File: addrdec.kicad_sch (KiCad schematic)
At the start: 5 parts, among them U10 74LS138, U11 74HCT00, U5 74HCT02, U8 74LS04, U9 74LS27

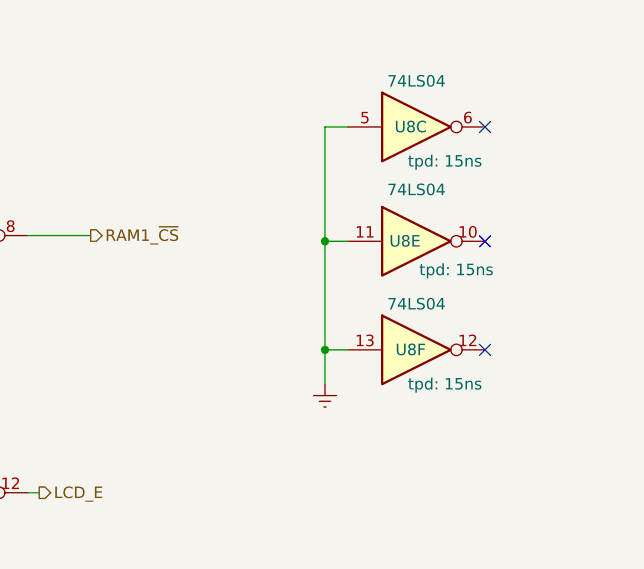
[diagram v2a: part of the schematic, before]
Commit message: fixed bugs in IRQ prio circuit
POST pass
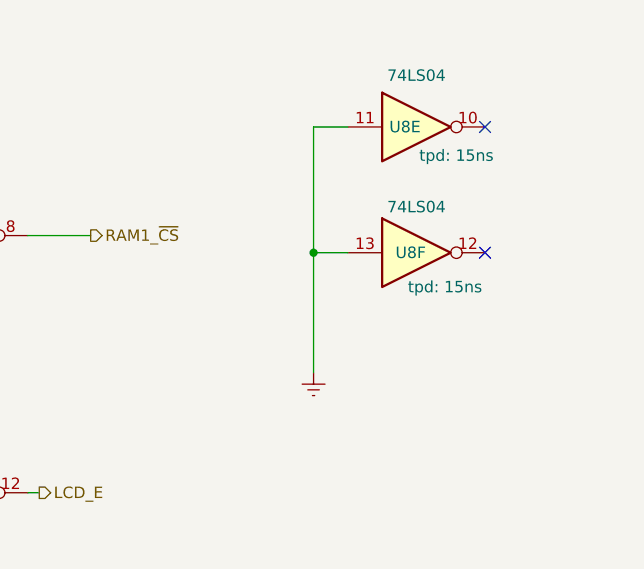
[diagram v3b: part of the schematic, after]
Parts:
- removed unit 3 of U8
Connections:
- no-connect marks 3 -> 2
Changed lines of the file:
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@@
 (kicad_sch (version 20230121) (generator eeschema)
   (paper "A4")
-  (junction (at 151.13 41.91) (diameter 0) (color 0 0 0 0)
-  )
   (junction (at 33.02 48.26) (diameter 0) (color 0 0 0 0)
   )
@@
   (junction (at 52.07 77.47) (diameter 0) (color 0 0 0 0)
   )
-  (junction (at 151.13 53.975) (diameter 0) (color 0 0 0 0)
-  )
   (junction (at 75.565 24.13) (diameter 0) (color 0 0 0 0)
   )
+  (junction (at 149.86 43.18) (diameter 0) (color 0 0 0 0)
+  )
   (junction (at 73.025 43.815) (diameter 0) (color 0 0 0 0)
   )
@@
   (junction (at 147.32 99.695) (diameter 0) (color 0 0 0 0)
   )
-  (no_connect (at 168.91 53.975))
-  (no_connect (at 168.91 41.91))
   (no_connect (at 168.91 29.21))
+  (no_connect (at 168.91 43.18))
   (bus_entry (at 27.94 82.55) (size 2.54 -2.54)
     (stroke (width 0) (type default))
@@
     (stroke (width 0) (type default))
   )
+  (wire (pts (xy 149.86 43.18) (xy 153.67 43.18))
+    (stroke (width 0) (type default))
+  )
   (bus (pts (xy 27.94 72.39) (xy 27.94 77.47))
     (stroke (width 0) (type default) (color 27 101 1 1))
@@
     (stroke (width 0) (type default))
   )
-  (wire (pts (xy 153.67 29.21) (xy 151.13 29.21))
+  (wire (pts (xy 153.67 29.21) (xy 149.86 29.21))
     (stroke (width 0) (type default))
   )
@@
   )
   (wire (pts (xy 82.55 72.39) (xy 102.87 72.39))
-    (stroke (width 0) (type default))
-  )
-  (wire (pts (xy 153.67 53.975) (xy 151.13 53.975))
     (stroke (width 0) (type default))
   )
@@
     (stroke (width 0) (type default))
   )
-  (wire (pts (xy 151.13 29.21) (xy 151.13 41.91))
+  (wire (pts (xy 149.86 43.18) (xy 149.86 56.515))
+    (stroke (width 0) (type default))
+  )
+  (wire (pts (xy 149.86 29.21) (xy 149.86 43.18))
     (stroke (width 0) (type default))
   )
@@
     (stroke (width 0) (type default))
   )
-  (wire (pts (xy 151.13 41.91) (xy 153.67 41.91))
-    (stroke (width 0) (type default))
-  )
   (wire (pts (xy 35.56 24.13) (xy 35.56 54.61))
     (stroke (width 0) (type default))
@@
     (stroke (width 0) (type default))
   )
-  (wire (pts (xy 151.13 53.975) (xy 151.13 57.785))
-    (stroke (width 0) (type default))
-  )
   (wire (pts (xy 62.865 24.13) (xy 75.565 24.13))
     (stroke (width 0) (type default))
@@
   )
   (wire (pts (xy 75.565 41.275) (xy 78.74 41.275))
-    (stroke (width 0) (type default))
-  )
-  (wire (pts (xy 151.13 41.91) (xy 151.13 53.975))
     (stroke (width 0) (type default))
   )
@@
     (effects (font (size 1.27 1.27)) (justify left))
   )
-  (hierarchical_label "LCD_E" (shape output) (at 119.38 69.85 0) (fields_autoplaced)
+  (hierarchical_label "LCD_E" (shape output) (at 119.38 69.85 0)
     (effects (font (size 1.27 1.27)) (justify left))
+    (property "tpd_LH" "56ns" (at 118.11 72.39 0) (show_name)
+      (effects (font (size 1.27 1.27) italic) (justify left))
+    )
+    (property "tpd_HL" "15ns" (at 118.11 74.041 0) (show_name)
+      (effects (font (size 1.27 1.27) italic) (justify left))
+    )
   )
   (hierarchical_label "DEV2_~{CS}" (shape output) (at 87.63 80.01 0) (fields_autoplaced)
@@
     )
   )
+  (symbol (lib_id "74xx:74LS04") (at 161.29 43.18 0) (unit 6)
+    (in_bom yes) (on_board yes) (dnp no)
+    (property "Reference" "U8" (at 160.655 43.18 0)
+      (effects (font (size 1.27 1.27)))
+    )
+    (property "Value" "74LS04" (at 161.29 38.1 0)
+      (effects (font (size 1.27 1.27)))
+    )
+    (property "Footprint" "" (at 161.29 43.18 0)
+      (effects (font (size 1.27 1.27)) hide)
+    )
+    (property "Datasheet" "http://www.ti.com/lit/gpn/sn74LS04" (at 161.29 43.18 0)
+      (effects (font (size 1.27 1.27)) hide)
+    )
+    (property "tpd" "15ns" (at 164.465 46.99 0) (show_name)
+      (effects (font (size 1.27 1.27)))
+    )
+    (pin "1")
+    (pin "2")
+    (pin "3")
+    (pin "4")
+    (pin "5")
+    (pin "6")
+    (pin "8")
+    (pin "9")
+    (pin "10")
+    (pin "11")
+    (pin "12")
+    (pin "13")
+    (pin "14")
+    (pin "7")
+    (instances
+      (project "rod6502"
+        (path "/031ea57b-8d17-4b45-87cc-c58302485ce1/4032fa43-c28c-4c35-b0ce-d5d9da6e84af"
+          (reference "U8") (unit 6)
+        )
+        (path "/031ea57b-8d17-4b45-87cc-c58302485ce1/890f0003-2042-459e-ac4a-1dd81f8fbcc6"
+          (reference "U8") (unit 6)
+        )
+      )
+    )
+  )
   (symbol (lib_id "74xx:74LS27") (at 43.18 77.47 0) (unit 2)
     (in_bom yes) (on_board yes) (dnp no)
@@
     )
   )
-  (symbol (lib_id "power:Earth") (at 151.13 57.785 0) (unit 1)
+  (symbol (lib_id "power:Earth") (at 149.86 56.515 0) (unit 1)
     (in_bom yes) (on_board yes) (dnp no) (fields_autoplaced)
-    (property "Reference" "#PWR044" (at 151.13 64.135 0)
-      (effects (font (size 1.27 1.27)) hide)
-    )
-    (property "Value" "Earth" (at 151.13 61.595 0)
-      (effects (font (size 1.27 1.27)) hide)
-    )
-    (property "Footprint" "" (at 151.13 57.785 0)
-      (effects (font (size 1.27 1.27)) hide)
-    )
-    (property "Datasheet" "~" (at 151.13 57.785 0)
+    (property "Reference" "#PWR044" (at 149.86 62.865 0)
+      (effects (font (size 1.27 1.27)) hide)
+    )
+    (property "Value" "Earth" (at 149.86 60.325 0)
+      (effects (font (size 1.27 1.27)) hide)
+    )
+    (property "Footprint" "" (at 149.86 56.515 0)
+      (effects (font (size 1.27 1.27)) hide)
+    )
+    (property "Datasheet" "~" (at 149.86 56.515 0)
       (effects (font (size 1.27 1.27)) hide)
     )
@@
     )
   )
-  (symbol (lib_id "74xx:74LS04") (at 161.29 41.91 0) (unit 5)
-    (in_bom yes) (on_board yes) (dnp no)
-    (property "Reference" "U8" (at 160.02 41.91 0)
-      (effects (font (size 1.27 1.27)))
-    )
-    (property "Value" "74LS04" (at 161.29 36.195 0)
-      (effects (font (size 1.27 1.27)))
-    )
-    (property "Footprint" "" (at 161.29 41.91 0)
-      (effects (font (size 1.27 1.27)) hide)
-    )
-    (property "Datasheet" "http://www.ti.com/lit/gpn/sn74LS04" (at 161.29 41.91 0)
-      (effects (font (size 1.27 1.27)) hide)
-    )
-    (property "tpd" "15ns" (at 165.735 45.085 0) (show_name)
-      (effects (font (size 1.27 1.27)))
-    )
-    (pin "1")
-    (pin "2")
-    (pin "3")
-    (pin "4")
-    (pin "5")
-    (pin "6")
-    (pin "8")
-    (pin "9")
-    (pin "10")
-    (pin "11")
-    (pin "12")
-    (pin "13")
-    (pin "14")
-    (pin "7")
-    (instances
-      (project "rod6502"
-        (path "/031ea57b-8d17-4b45-87cc-c58302485ce1/4032fa43-c28c-4c35-b0ce-d5d9da6e84af"
-          (reference "U8") (unit 5)
-        )
-        (path "/031ea57b-8d17-4b45-87cc-c58302485ce1/890f0003-2042-459e-ac4a-1dd81f8fbcc6"
-          (reference "U8") (unit 5)
-        )
-      )
-    )
-  )
   (symbol (lib_id "74xx:74LS04") (at 55.245 24.13 0) (unit 1)
     (in_bom yes) (on_board yes) (dnp no)
@@
     )
   )
-  (symbol (lib_id "74xx:74LS04") (at 161.29 53.975 0) (unit 6)
-    (in_bom yes) (on_board yes) (dnp no)
-    (property "Reference" "U8" (at 160.655 53.975 0)
-      (effects (font (size 1.27 1.27)))
-    )
-    (property "Value" "74LS04" (at 161.29 48.895 0)
-      (effects (font (size 1.27 1.27)))
-    )
-    (property "Footprint" "" (at 161.29 53.975 0)
-      (effects (font (size 1.27 1.27)) hide)
-    )
-    (property "Datasheet" "http://www.ti.com/lit/gpn/sn74LS04" (at 161.29 53.975 0)
-      (effects (font (size 1.27 1.27)) hide)
-    )
-    (property "tpd" "15ns" (at 164.465 57.785 0) (show_name)
-      (effects (font (size 1.27 1.27)))
-    )
-    (pin "1")
-    (pin "2")
-    (pin "3")
-    (pin "4")
-    (pin "5")
-    (pin "6")
-    (pin "8")
-    (pin "9")
-    (pin "10")
-    (pin "11")
-    (pin "12")
-    (pin "13")
-    (pin "14")
-    (pin "7")
-    (instances
-      (project "rod6502"
-        (path "/031ea57b-8d17-4b45-87cc-c58302485ce1/4032fa43-c28c-4c35-b0ce-d5d9da6e84af"
-          (reference "U8") (unit 6)
-        )
-      )
-    )
-  )
   (symbol (lib_id "power:VCC") (at 69.85 55.88 0) (unit 1)
     (in_bom yes) (on_board yes) (dnp no) (fields_autoplaced)
@@
     )
   )
-  (symbol (lib_id "74xx:74LS04") (at 161.29 29.21 0) (unit 3)
-    (in_bom yes) (on_board yes) (dnp no)
-    (property "Reference" "U8" (at 160.655 29.21 0)
-      (effects (font (size 1.27 1.27)))
-    )
-    (property "Value" "74LS04" (at 161.29 24.13 0)
+  (symbol (lib_id "74xx:74LS04") (at 161.29 29.21 0) (unit 5)
+    (in_bom yes) (on_board yes) (dnp no)
+    (property "Reference" "U8" (at 160.02 29.21 0)
+      (effects (font (size 1.27 1.27)))
+    )
+    (property "Value" "74LS04" (at 161.29 23.495 0)
       (effects (font (size 1.27 1.27)))
     )
@@
       (effects (font (size 1.27 1.27)) hide)
     )
-    (property "tpd" "15ns" (at 164.465 33.02 0) (show_name)
-      (effects (font (size 1.27 1.27)))
-    )
-    (pin "1")
-    (pin "2")
-    (pin "3")
-    (pin "4")
-    (pin "5")
-    (pin "6")
-    (pin "8")
-    (pin "9")
-    (pin "10")
-    (pin "11")
-    (pin "12")
-    (pin "13")
-    (pin "14")
-    (pin "7")
-    (instances
-      (project "rod6502"
-        (path "/031ea57b-8d17-4b45-87cc-c58302485ce1/4032fa43-c28c-4c35-b0ce-d5d9da6e84af"
-          (reference "U8") (unit 3)
+    (property "tpd" "15ns" (at 165.735 32.385 0) (show_name)
+      (effects (font (size 1.27 1.27)))
+    )
+    (pin "1")
+    (pin "2")
+    (pin "3")
+    (pin "4")
+    (pin "5")
+    (pin "6")
+    (pin "8")
+    (pin "9")
+    (pin "10")
+    (pin "11")
+    (pin "12")
+    (pin "13")
+    (pin "14")
+    (pin "7")
+    (instances
+      (project "rod6502"
+        (path "/031ea57b-8d17-4b45-87cc-c58302485ce1/4032fa43-c28c-4c35-b0ce-d5d9da6e84af"
+          (reference "U8") (unit 5)
         )
         (path "/031ea57b-8d17-4b45-87cc-c58302485ce1/890f0003-2042-459e-ac4a-1dd81f8fbcc6"
-          (reference "U8") (unit 3)
-        )
-      )
+          (reference "U8") (unit 5)
+        )
+      )

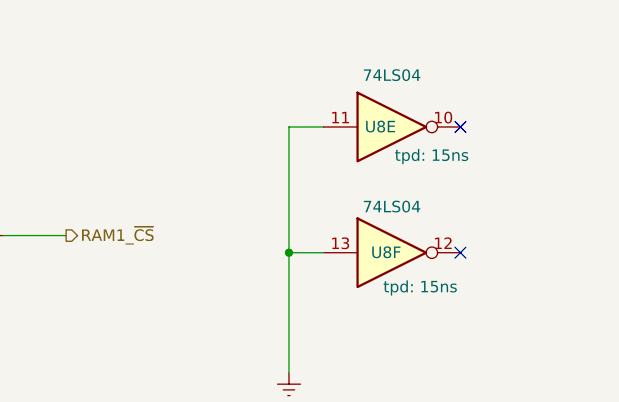
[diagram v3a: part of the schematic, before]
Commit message: output POST status on lcd display
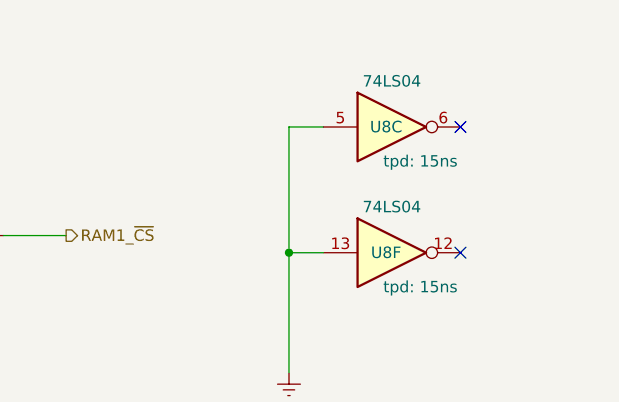
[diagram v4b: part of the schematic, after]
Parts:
- removed unit 5 of U8
- added unit 3 of U8
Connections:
- net Earth: now also U8.5
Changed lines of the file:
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@@
+    )
+  )
+  (symbol (lib_id "74xx:74LS04") (at 161.29 29.21 0) (unit 3)
+    (in_bom yes) (on_board yes) (dnp no)
+    (property "Reference" "U8" (at 160.655 29.21 0)
+      (effects (font (size 1.27 1.27)))
+    )
+    (property "Value" "74LS04" (at 161.29 24.13 0)
+      (effects (font (size 1.27 1.27)))
+    )
+    (property "Footprint" "" (at 161.29 29.21 0)
+      (effects (font (size 1.27 1.27)) hide)
+    )
+    (property "Datasheet" "http://www.ti.com/lit/gpn/sn74LS04" (at 161.29 29.21 0)
+      (effects (font (size 1.27 1.27)) hide)
+    )
+    (property "tpd" "15ns" (at 164.465 33.02 0) (show_name)
+      (effects (font (size 1.27 1.27)))
+    )
+    (pin "1")
+    (pin "2")
+    (pin "3")
+    (pin "4")
+    (pin "5")
+    (pin "6")
+    (pin "8")
+    (pin "9")
+    (pin "10")
+    (pin "11")
+    (pin "12")
+    (pin "13")
+    (pin "14")
+    (pin "7")
+    (instances
+      (project "rod6502"
+        (path "/031ea57b-8d17-4b45-87cc-c58302485ce1/4032fa43-c28c-4c35-b0ce-d5d9da6e84af"
+          (reference "U8") (unit 3)
+        )
+        (path "/031ea57b-8d17-4b45-87cc-c58302485ce1/890f0003-2042-459e-ac4a-1dd81f8fbcc6"
+          (reference "U8") (unit 3)
+        )
+      )
     )
   )
@@
         )
       )
-    )
-  )
-  (symbol (lib_id "74xx:74LS04") (at 161.29 29.21 0) (unit 5)
-    (in_bom yes) (on_board yes) (dnp no)
-    (property "Reference" "U8" (at 160.02 29.21 0)
-      (effects (font (size 1.27 1.27)))
-    )
-    (property "Value" "74LS04" (at 161.29 23.495 0)
-      (effects (font (size 1.27 1.27)))
-    )
-    (property "Footprint" "" (at 161.29 29.21 0)
-      (effects (font (size 1.27 1.27)) hide)
-    )
-    (property "Datasheet" "http://www.ti.com/lit/gpn/sn74LS04" (at 161.29 29.21 0)
-      (effects (font (size 1.27 1.27)) hide)
-    )
-    (property "tpd" "15ns" (at 165.735 32.385 0) (show_name)
-      (effects (font (size 1.27 1.27)))
-    )
-    (pin "1")
-    (pin "2")
-    (pin "3")
-    (pin "4")
-    (pin "5")
-    (pin "6")
-    (pin "8")
-    (pin "9")
-    (pin "10")
-    (pin "11")
-    (pin "12")
-    (pin "13")
-    (pin "14")
-    (pin "7")
-    (instances
-      (project "rod6502"
-        (path "/031ea57b-8d17-4b45-87cc-c58302485ce1/4032fa43-c28c-4c35-b0ce-d5d9da6e84af"
-          (reference "U8") (unit 5)
-        )
-        (path "/031ea57b-8d17-4b45-87cc-c58302485ce1/890f0003-2042-459e-ac4a-1dd81f8fbcc6"
-          (reference "U8") (unit 5)
-        )
-      )
